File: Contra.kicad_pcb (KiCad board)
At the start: 2 copper layers, 251.5 x 76.2 mm, 152 parts, among them J1 Conn_01x03, J2 Conn_01x02, SW1 SW_PUSH, SW2 SW_SPDT, U1 ProMicro

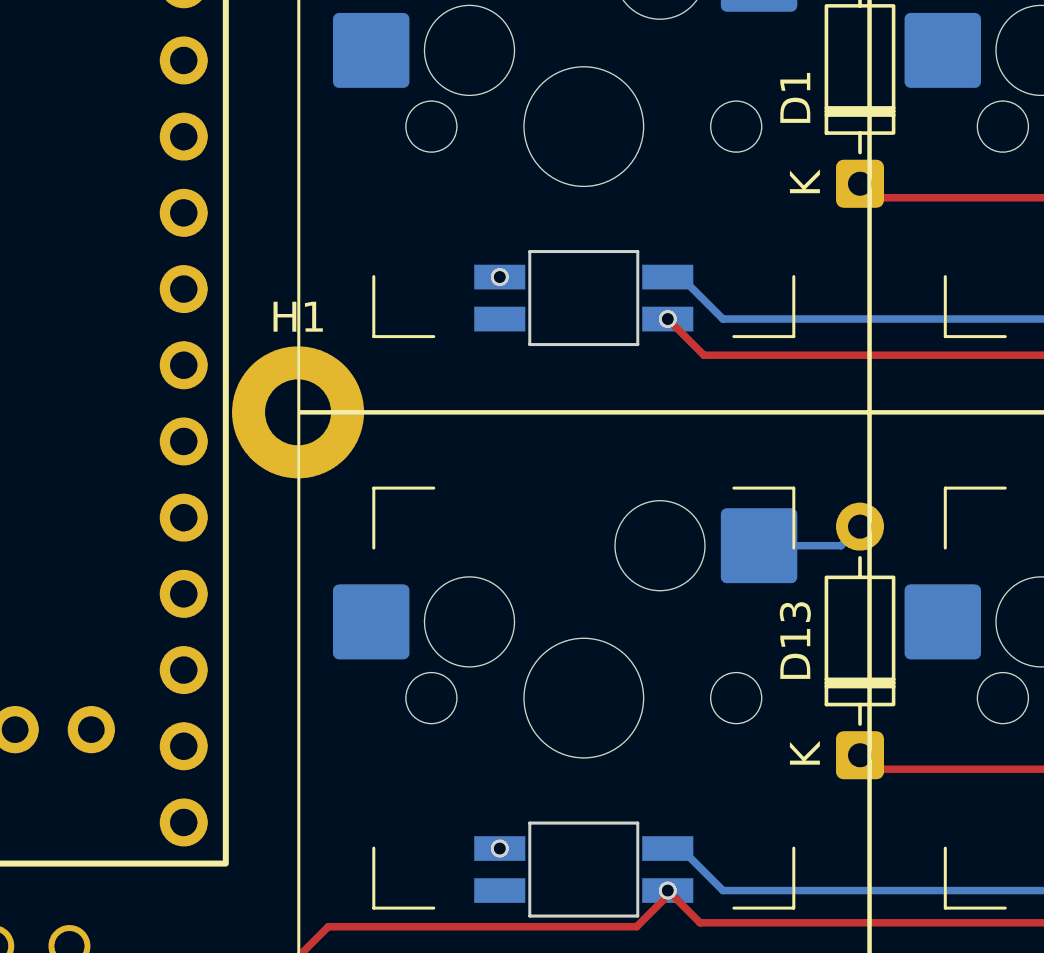
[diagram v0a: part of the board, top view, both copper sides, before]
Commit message: connect row0 and row1 to mcu
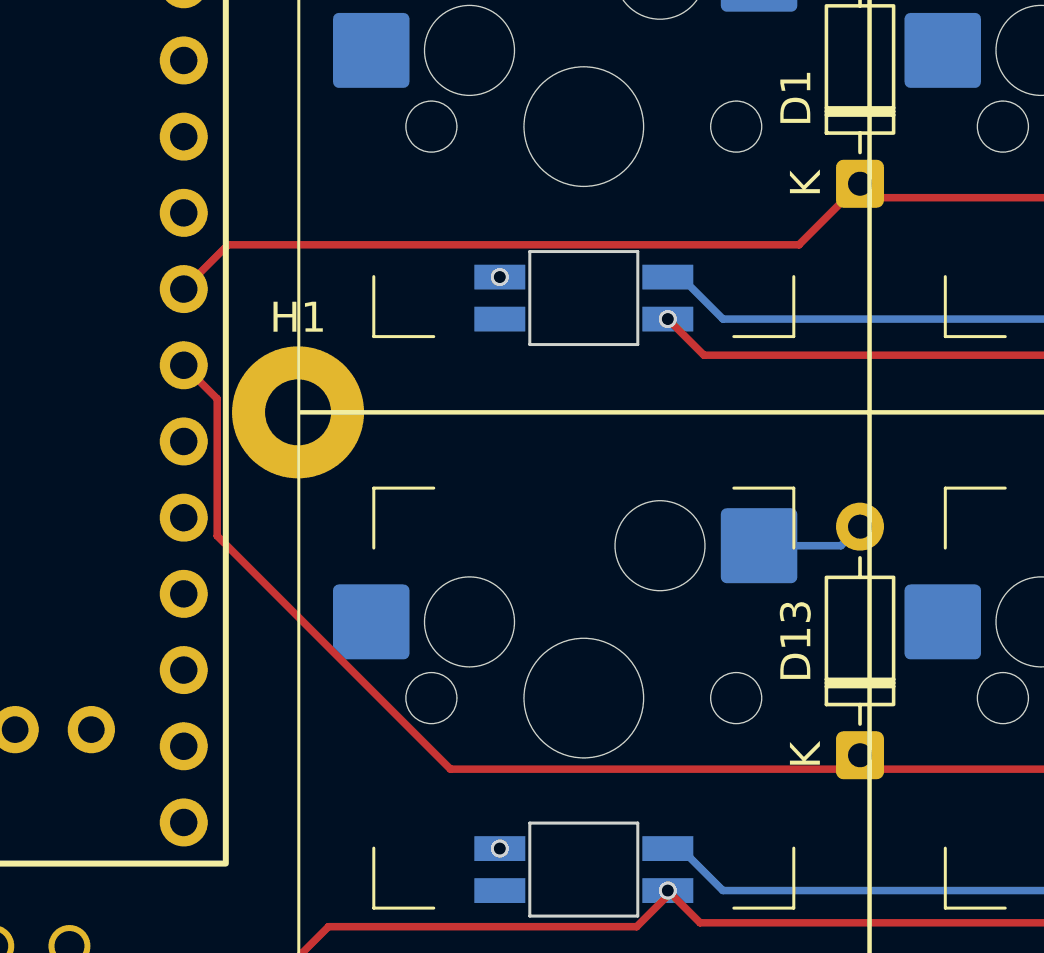
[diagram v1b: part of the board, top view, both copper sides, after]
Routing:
- net ROW1: track 199.3 -> 229.7 mm
- net ROW0: track 199.3 -> 223.3 mm
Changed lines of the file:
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@@
+	)
+	(segment
+		(start 61.465 64.9)
+		(end 42.433041 64.9)
+		(width 0.25)
+		(layer "F.Cu")
+		(net "ROW0")
 	)
 	(segment
@@
 	)
 	(segment
+		(start 63.5 62.865)
+		(end 61.465 64.9)
+		(width 0.25)
+		(layer "F.Cu")
+		(net "ROW0")
+	)
+	(segment
 		(start 196.3861 63.3289)
 		(end 178.2639 63.3289)
@@
 	)
 	(segment
+		(start 42.433041 64.9)
+		(end 40.95751 66.375531)
+		(width 0.25)
+		(layer "F.Cu")
+		(net "ROW0")
+	)
+	(segment
 		(start 234.4861 63.3289)
 		(end 216.3639 63.3289)
@@
 	)
 	(segment
+		(start 42.07251 74.603694)
+		(end 42.07251 70.030531)
+		(width 0.25)
+		(layer "F.Cu")
+		(net "ROW1")
+	)
+	(segment
 		(start 159.2139 82.3789)
 		(end 177.3361 82.3789)
@@
 	)
 	(segment
+		(start 63.0361 82.3789)
+		(end 49.847716 82.3789)
+		(width 0.25)
+		(layer "F.Cu")
+		(net "ROW1")
+	)
+	(segment
 		(start 197.3139 82.3789)
 		(end 215.4361 82.3789)
@@
 	)
 	(segment
+		(start 49.847716 82.3789)
+		(end 42.07251 74.603694)
+		(width 0.25)
+		(layer "F.Cu")
+		(net "ROW1")
+	)
+	(segment
 		(start 235.4139 82.3789)
 		(end 253.5361 82.3789)
@@
 		(width 0.25)
 		(layer "F.Cu")
+		(net "ROW1")
+	)
+	(segment
+		(start 42.07251 70.030531)
+		(end 40.95751 68.915531)
+		(width 0.25)
+		(layer "F.Cu")

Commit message: connect led din to mcu, connect col0
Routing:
- net COL0: track 0.00 -> 62.2 mm
- net NeopixelDin: track 0.00 -> 22.9 mm
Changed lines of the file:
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@@
 		(net "Net-(D47-A)")
+	)
+	(segment
+		(start 40.95751 76.535531)
+		(end 46.273031 76.535531)
+		(width 0.25)
+		(layer "B.Cu")
+		(net "COL0")
+	)
+	(segment
+		(start 47.2825 58.495)
+		(end 47.2825 77.395)
+		(width 0.25)
+		(layer "B.Cu")
+		(net "COL0")
+	)
+	(segment
+		(start 47.2075 96.52)
+		(end 47.2075 77.47)
+		(width 0.25)
+		(layer "B.Cu")
+		(net "COL0")
+	)
+	(segment
+		(start 47.2825 115.495)
+		(end 47.2825 96.595)
+		(width 0.25)
+		(layer "B.Cu")
+		(net "COL0")
 	)
 	(via
@@
 	)
 	(segment
+		(start 40.95751 56.215531)
+		(end 50.929681 56.215531)
+		(width 0.25)
+		(layer "B.Cu")
+		(net "NeopixelDin")
+	)
+	(segment
+		(start 50.3275 64.925)
+		(end 50.3275 66.6475)
+		(width 0.25)
+		(layer "B.Cu")
+		(net "NeopixelDin")
+	)
+	(segment
+		(start 50.4825 64.77)
+		(end 50.3275 64.925)
+		(width 0.25)
+		(layer "B.Cu")
+		(net "NeopixelDin")
+	)
+	(segment
+		(start 50.929681 56.215531)
+		(end 52.3875 57.67335)
+		(width 0.25)
+		(layer "B.Cu")
+		(net "NeopixelDin")
+	)
+	(segment
+		(start 50.4825 61.419869)
+		(end 50.4825 64.77)
+		(width 0.25)
+		(layer "B.Cu")
+		(net "NeopixelDin")
+	)
+	(segment
+		(start 52.3875 57.67335)
+		(end 52.3875 59.514869)
+		(width 0.25)
+		(layer "B.Cu")
+		(net "NeopixelDin")
+	)
+	(segment
+		(start 52.3875 59.514869)
+		(end 50.4825 61.419869)
+		(width 0.25)
+		(layer "B.Cu")
+		(net "NeopixelDin")
+	)
+	(segment
+		(start 50.3275 66.6475)
+		(end 51.055 67.375)
+		(width 0.25)
+		(layer "B.Cu")
+		(net "NeopixelDin")
+	)
+	(segment

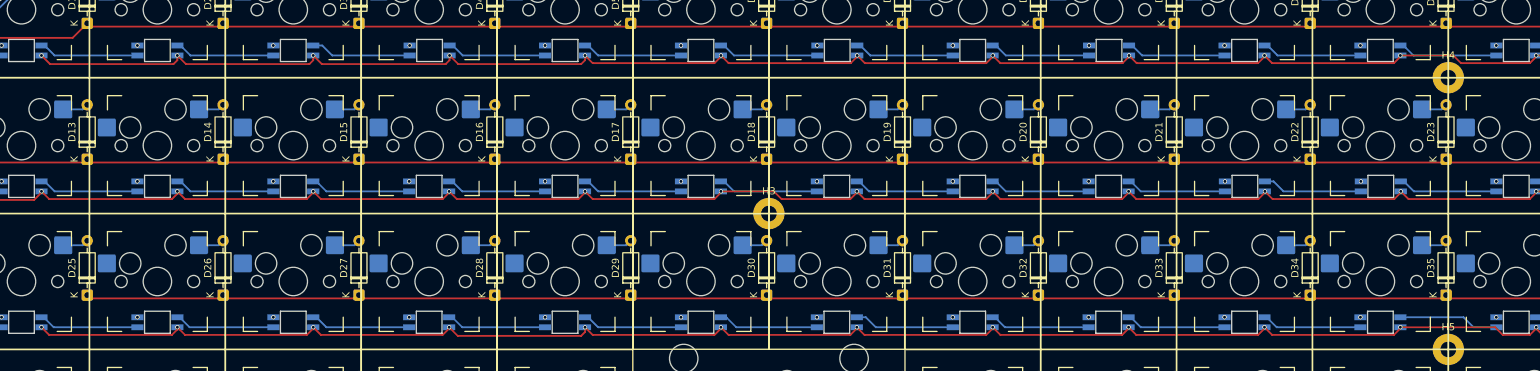
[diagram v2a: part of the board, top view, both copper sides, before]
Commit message: adjust led data tracks for better spacing
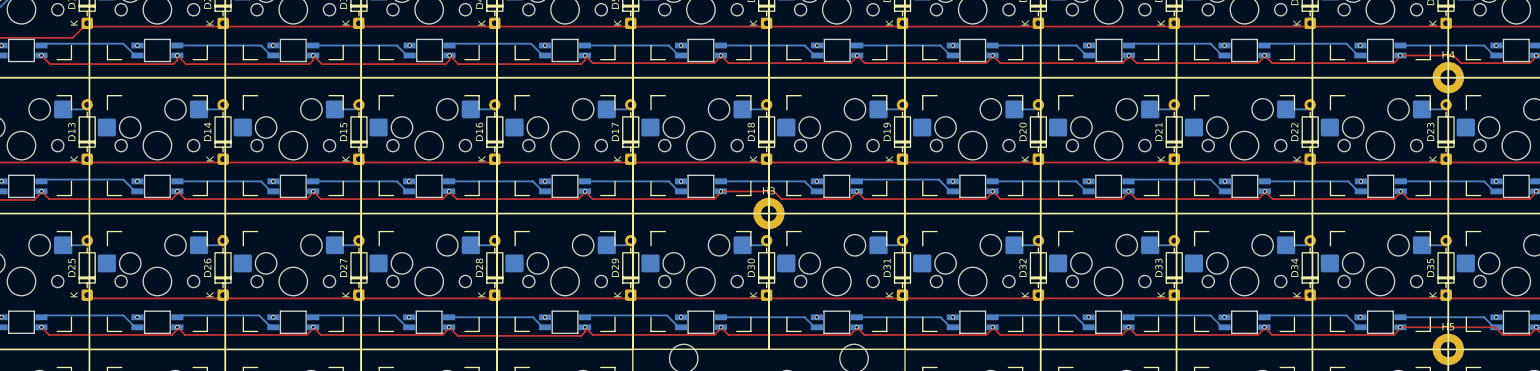
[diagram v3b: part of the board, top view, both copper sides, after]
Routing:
- net Net-(LED21-DOUT): track 13.8 -> 13.3 mm

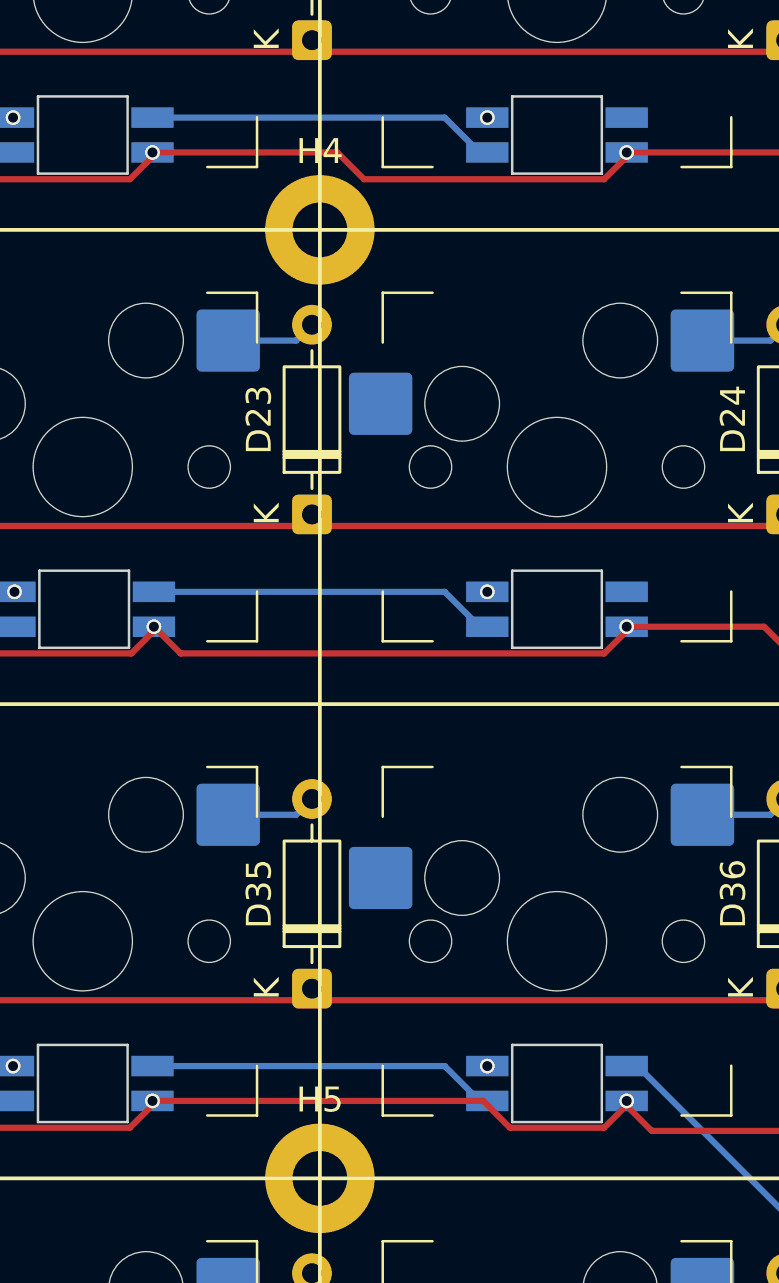
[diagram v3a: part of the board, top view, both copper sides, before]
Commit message: tweak power track placement
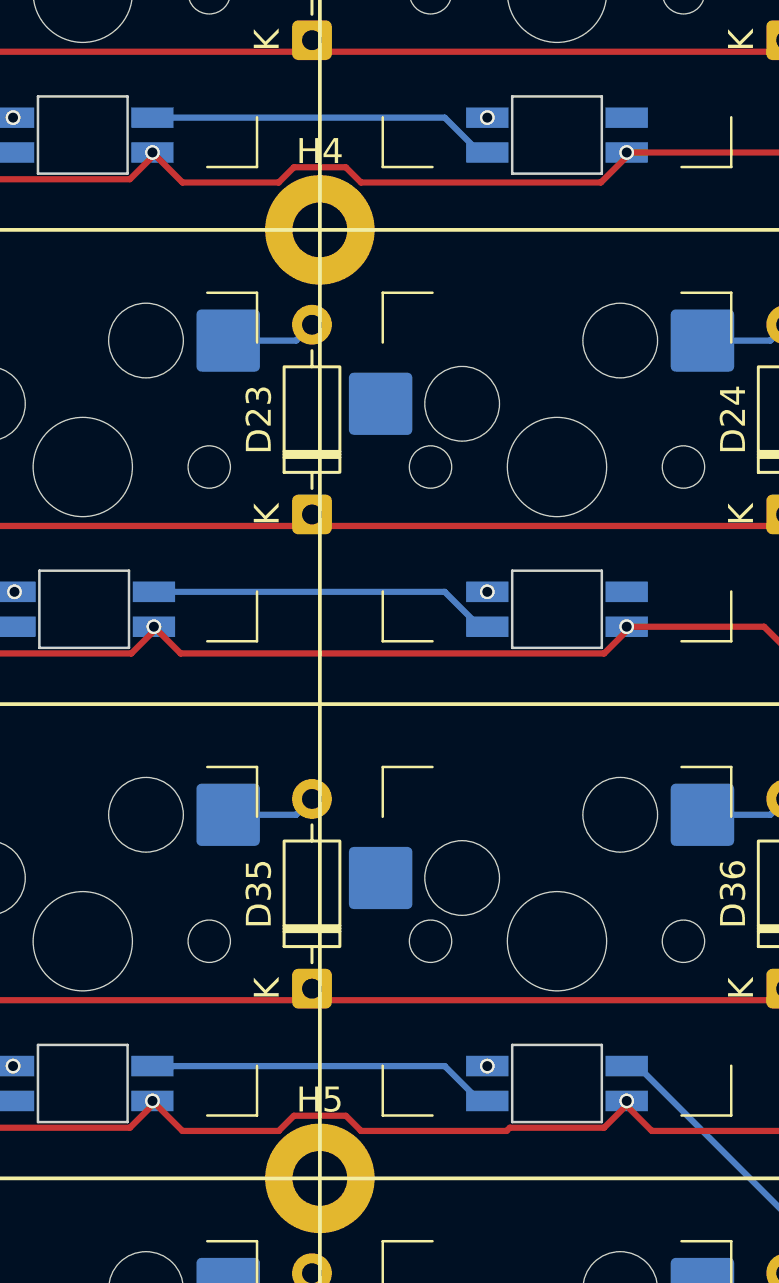
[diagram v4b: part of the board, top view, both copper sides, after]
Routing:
- net VBAT: track 1112.4 -> 1113.6 mm

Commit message: connect col11
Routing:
- net COL11: track 0.00 -> 56.4 mm, vias 0 -> 6
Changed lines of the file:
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@@
 		(net "COL0")
+	)
+	(segment
+		(start 257.175 64.77)
+		(end 257.175 66.675)
+		(width 0.25)
+		(layer "F.Cu")
+		(net "COL11")
+	)
+	(segment
+		(start 257.175 83.82)
+		(end 257.175 85.725)
+		(width 0.25)
+		(layer "F.Cu")
+		(net "COL11")
+	)
+	(segment
+		(start 257.175 102.87)
+		(end 257.175 104.775)
+		(width 0.25)
+		(layer "F.Cu")
+		(net "COL11")
+	)
+	(via
+		(at 257.175 102.87)
+		(size 0.6)
+		(drill 0.4)
+		(layers "F.Cu" "B.Cu")
+		(net "COL11")
+	)
+	(via
+		(at 257.175 83.82)
+		(size 0.6)
+		(drill 0.4)
+		(layers "F.Cu" "B.Cu")
+		(net "COL11")
+	)
+	(via
+		(at 257.175 104.775)
+		(size 0.6)
+		(drill 0.4)
+		(layers "F.Cu" "B.Cu")
+		(net "COL11")
+	)
+	(via
+		(at 257.175 64.77)
+		(size 0.6)
+		(drill 0.4)
+		(layers "F.Cu" "B.Cu")
+		(net "COL11")
+	)
+	(via
+		(at 257.175 85.725)
+		(size 0.6)
+		(drill 0.4)
+		(layers "F.Cu" "B.Cu")
+		(net "COL11")
+	)
+	(via
+		(at 257.175 66.675)
+		(size 0.6)
+		(drill 0.4)
+		(layers "F.Cu" "B.Cu")
+		(net "COL11")
+	)
+	(segment
+		(start 257.175 96.9375)
+		(end 257.175 102.87)
+		(width 0.25)
+		(layer "B.Cu")
+		(net "COL11")
+	)
+	(segment
+		(start 257.175 88.5825)
+		(end 256.7575 89)
+		(width 0.25)
+		(layer "B.Cu")
+		(net "COL11")
+	)
+	(segment
+		(start 257.175 66.675)
+		(end 257.175 77.0525)
+		(width 0.25)
+		(layer "B.Cu")
+		(net "COL11")
+	)
+	(segment
+		(start 257.175 104.775)
+		(end 257.175 115.1525)
+		(width 0.25)
+		(layer "B.Cu")
+		(net "COL11")
+	)
+	(segment
+		(start 256.7575 77.47)
+		(end 256.7575 83.4025)
+		(width 0.25)
+		(layer "B.Cu")
+		(net "COL11")
+	)
+	(segment
+		(start 256.7575 64.3525)
+		(end 257.175 64.77)
+		(width 0.25)
+		(layer "B.Cu")
+		(net "COL11")
+	)
+	(segment
+		(start 256.7575 89)
+		(end 256.7575 96.52)
+		(width 0.25)
+		(layer "B.Cu")
+		(net "COL11")
+	)
+	(segment
+		(start 256.7575 83.4025)
+		(end 257.175 83.82)
+		(width 0.25)
+		(layer "B.Cu")
+		(net "COL11")
+	)
+	(segment
+		(start 257.175 85.725)
+		(end 257.175 88.5825)
+		(width 0.25)
+		(layer "B.Cu")
+		(net "COL11")
+	)
+	(segment
+		(start 256.7575 58.42)
+		(end 256.7575 64.3525)
+		(width 0.25)
+		(layer "B.Cu")
+		(net "COL11")
 	)
 	(via

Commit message: connect col10
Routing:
- net COL10: track 0.00 -> 58.2 mm, vias 0 -> 6
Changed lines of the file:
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@@
+	)
+	(segment
+		(start 238.125 83.82)
+		(end 238.125 85.725)
+		(width 0.25)
+		(layer "F.Cu")
+		(net "COL10")
+	)
+	(segment
+		(start 238.125 64.77)
+		(end 238.125 66.675)
+		(width 0.25)
+		(layer "F.Cu")
+		(net "COL10")
+	)
+	(segment
+		(start 238.125 102.87)
+		(end 238.125 104.775)
+		(width 0.25)
+		(layer "F.Cu")
+		(net "COL10")
+	)
+	(via
+		(at 238.125 83.82)
+		(size 0.6)
+		(drill 0.4)
+		(layers "F.Cu" "B.Cu")
+		(net "COL10")
+	)
+	(via
+		(at 238.125 102.87)
+		(size 0.6)
+		(drill 0.4)
+		(layers "F.Cu" "B.Cu")
+		(net "COL10")
+	)
+	(via
+		(at 238.125 66.675)
+		(size 0.6)
+		(drill 0.4)
+		(layers "F.Cu" "B.Cu")
+		(net "COL10")
+	)
+	(via
+		(at 238.125 104.775)
+		(size 0.6)
+		(drill 0.4)
+		(layers "F.Cu" "B.Cu")
+		(net "COL10")
+	)
+	(via
+		(at 238.125 64.77)
+		(size 0.6)
+		(drill 0.4)
+		(layers "F.Cu" "B.Cu")
+		(net "COL10")
+	)
+	(via
+		(at 238.125 85.725)
+		(size 0.6)
+		(drill 0.4)
+		(layers "F.Cu" "B.Cu")
+		(net "COL10")
+	)
+	(segment
+		(start 238.125 66.675)
+		(end 237.7075 67.0925)
+		(width 0.25)
+		(layer "B.Cu")
+		(net "COL10")
+	)
+	(segment
+		(start 237.7075 83.4025)
+		(end 238.125 83.82)
+		(width 0.25)
+		(layer "B.Cu")
+		(net "COL10")
+	)
+	(segment
+		(start 238.125 85.725)
+		(end 237.7075 86.1425)
+		(width 0.25)
+		(layer "B.Cu")
+		(net "COL10")
+	)
+	(segment
+		(start 237.7075 105.1925)
+		(end 237.7075 115.57)
+		(width 0.25)
+		(layer "B.Cu")
+		(net "COL10")
+	)
+	(segment
+		(start 237.7075 86.1425)
+		(end 237.7075 96.52)
+		(width 0.25)
+		(layer "B.Cu")
+		(net "COL10")
+	)
+	(segment
+		(start 238.125 104.775)
+		(end 237.7075 105.1925)
+		(width 0.25)
+		(layer "B.Cu")
+		(net "COL10")
+	)
+	(segment
+		(start 237.7075 102.4525)
+		(end 238.125 102.87)
+		(width 0.25)
+		(layer "B.Cu")
+		(net "COL10")
+	)
+	(segment
+		(start 237.7075 96.52)
+		(end 237.7075 102.4525)
+		(width 0.25)
+		(layer "B.Cu")
+		(net "COL10")
+	)
+	(segment
+		(start 237.7075 58.42)
+		(end 237.7075 64.3525)
+		(width 0.25)
+		(layer "B.Cu")
+		(net "COL10")
+	)
+	(segment
+		(start 237.7075 77.47)
+		(end 237.7075 83.4025)
+		(width 0.25)
+		(layer "B.Cu")
+		(net "COL10")
+	)
+	(segment
+		(start 237.7075 67.0925)
+		(end 237.7075 77.47)
+		(width 0.25)
+		(layer "B.Cu")
+		(net "COL10")
+	)
+	(segment
+		(start 237.7075 64.3525)
+		(end 238.125 64.77)
+		(width 0.25)
+		(layer "B.Cu")
+		(net "COL10")
 	)
 	(segment

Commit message: connect the rest of the collumns
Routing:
- net COL5: track 0.00 -> 63.6 mm, vias 0 -> 6
- net COL8: track 0.00 -> 58.2 mm, vias 0 -> 6
- net COL4: track 0.00 -> 58.2 mm, vias 0 -> 6
- net COL3: track 0.00 -> 58.2 mm, vias 0 -> 6
- net COL1: track 0.00 -> 58.2 mm, vias 0 -> 6
- net COL9: track 0.00 -> 58.2 mm, vias 0 -> 6
- net COL7: track 0.00 -> 58.2 mm, vias 0 -> 6
- net COL2: track 0.00 -> 58.2 mm, vias 0 -> 6
- net COL6: track 0.00 -> 38.2 mm, vias 0 -> 4
